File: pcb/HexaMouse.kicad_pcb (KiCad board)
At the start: 2 copper layers, 55 x 65.5 mm, 26 parts, among them J1 Conn_01x02_Socket, J2 Conn_01x02_Socket, J3 Xiao_Headers_Left, J4 Xiao_Headers_Right, SW1 SW_SPDT, U2 TLV493D, U3 TLV493D, U4 TLV493D, U5 TCA9548APWR

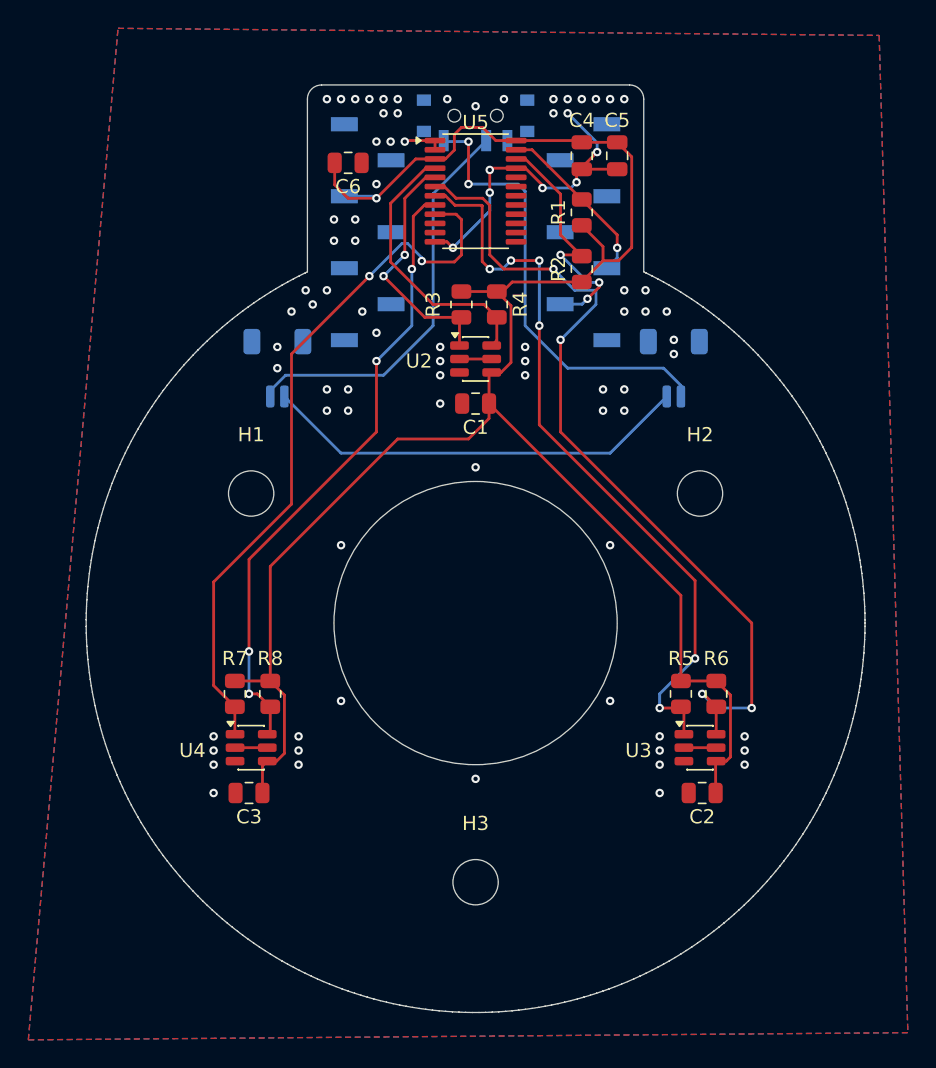
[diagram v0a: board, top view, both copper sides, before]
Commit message: Made power and ground traces wider
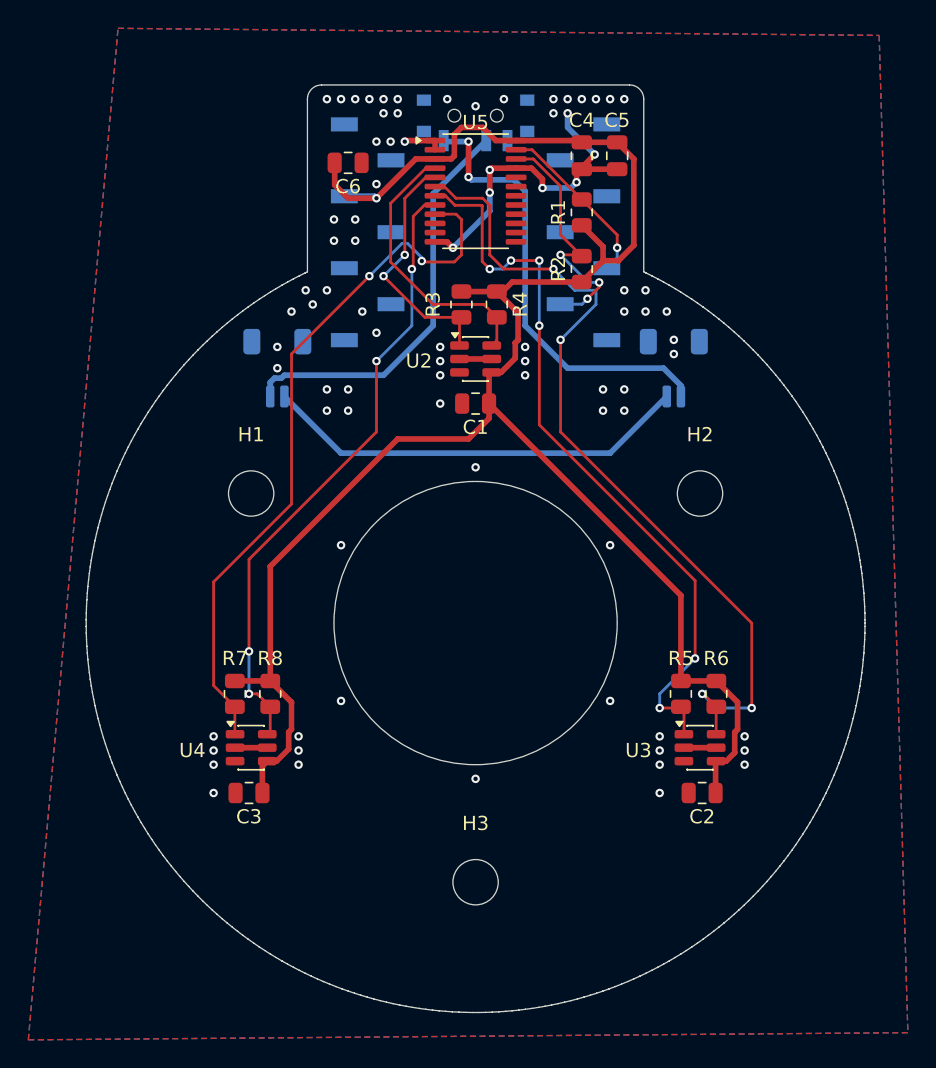
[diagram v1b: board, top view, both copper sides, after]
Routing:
- net +3.3V: track 138.7 -> 140.3 mm
